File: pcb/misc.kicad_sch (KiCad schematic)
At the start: 11 parts, among them U3 ESP32-C3-MINI-1

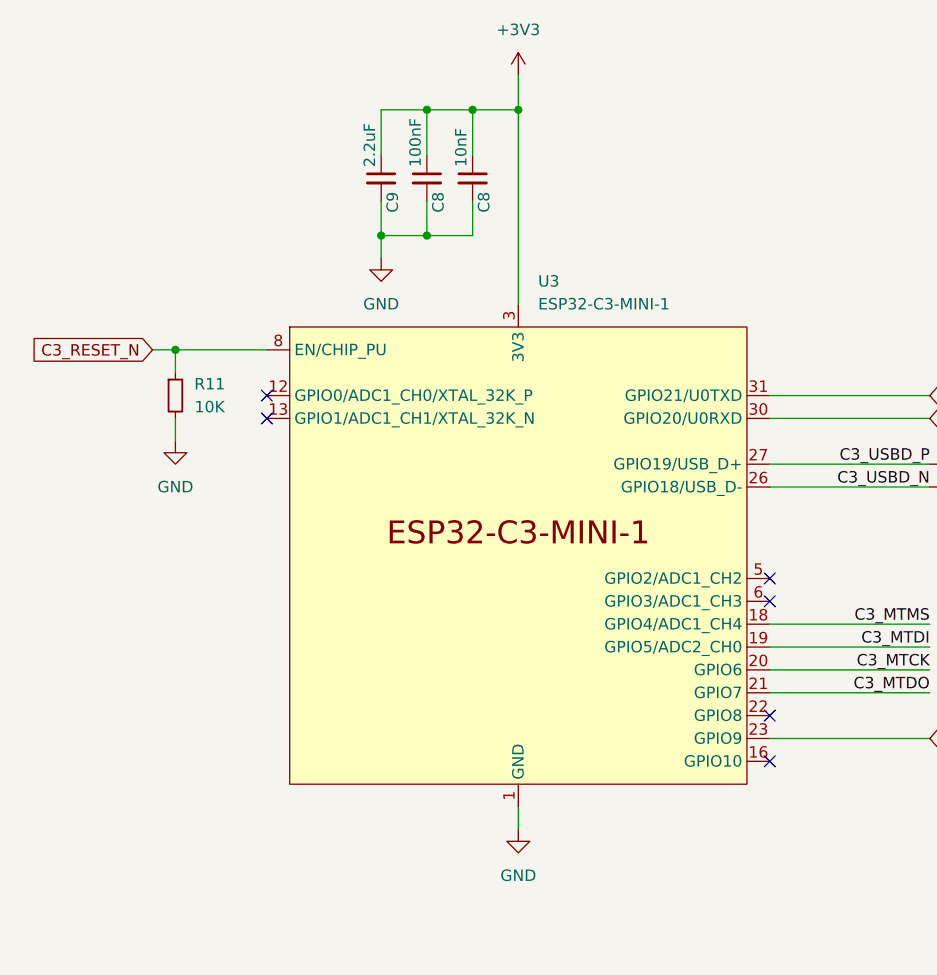
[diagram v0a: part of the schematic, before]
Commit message: pcb: Add part numbers for passives
Change-Id: Ie1730dd2a7126b7f6f602689064a4dbf8996e7b6
Reviewed-on: https://pigweed-review.googlesource.com/c/pigweed/kudzu/+/172895
Reviewed-by: Anthony DiGirolamo <anthony.digirolamo@gmail.com>
Reviewed-by: Anthony DiGirolamo <tonymd@google.com>
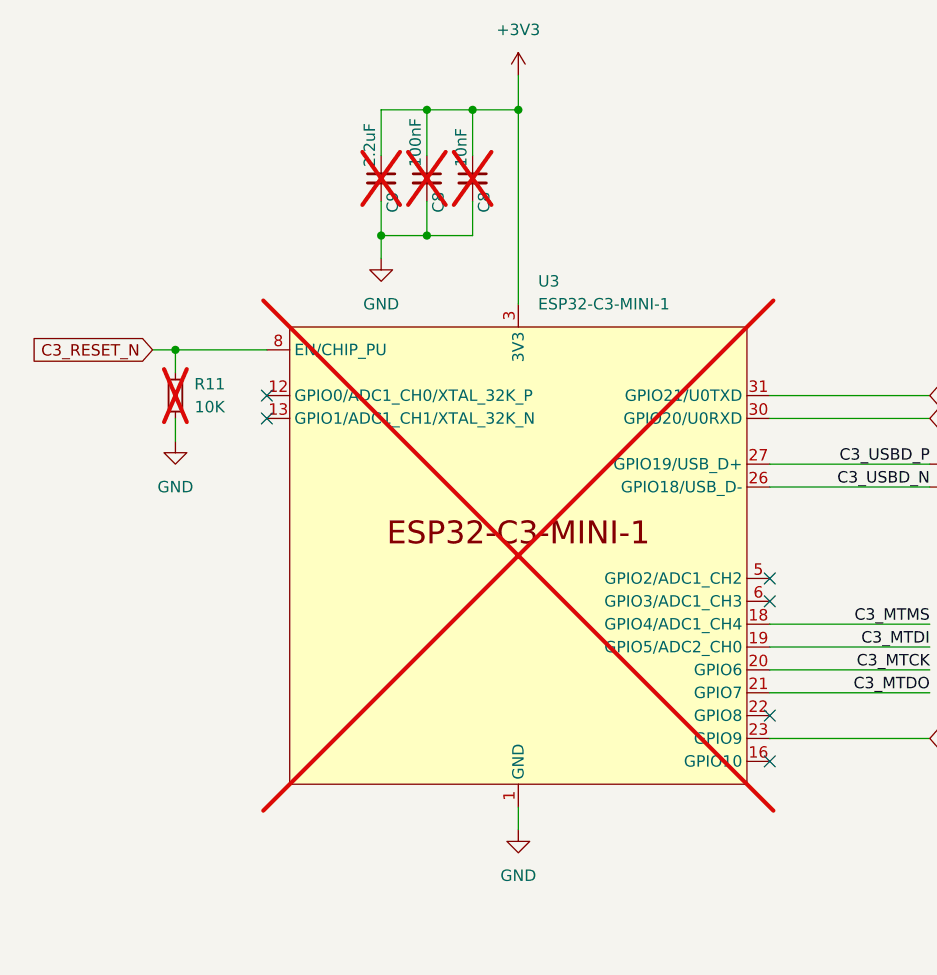
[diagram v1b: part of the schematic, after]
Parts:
- C8: DigiKey PN (none) -> 1276-1009-2-ND; Price @ 10 (none) -> 0.02500; Price @ 25 (none) -> 0.01340; now not fitted
- C8: DigiKey PN (none) -> 1276-1000-2-ND; Price @ 10 (none) -> 0.01200; Price @ 25 (none) -> 0.00856; now not fitted
- C9: DigiKey PN (none) -> 1276-1040-2-ND; Price @ 10 (none) -> 0.03460; Price @ 25 (none) -> 0.02830; now not fitted
- R11: DigiKey PN (none) -> RNCP0603FTD10K0TR-ND; Price @ 10 (none) -> 0.03240; Price @ 25 (none) -> 0.02380; now not fitted
- U3: now not fitted
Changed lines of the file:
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@@
   )
   (symbol (lib_id "Device:C_Small") (at 123.19 34.29 0) (unit 1)
-    (in_bom yes) (on_board yes) (dnp no)
+    (in_bom yes) (on_board yes) (dnp yes)
     (property "Reference" "C9" (at 124.46 38.1 90)
       (effects (font (size 1.27 1.27)) (justify left))
@@
       (effects (font (size 1.27 1.27)) hide)
     )
-    (property "Price @ 10" "" (at 123.19 34.29 0)
-      (effects (font (size 1.27 1.27)) hide)
-    )
-    (property "Price @ 25" "" (at 123.19 34.29 0)
+    (property "Price @ 10" "0.03460" (at 123.19 34.29 0)
+      (effects (font (size 1.27 1.27)) hide)
+    )
+    (property "Price @ 25" "0.02830" (at 123.19 34.29 0)
+      (effects (font (size 1.27 1.27)) hide)
+    )
+    (property "DigiKey PN" "1276-1040-2-ND" (at 123.19 34.29 0)
       (effects (font (size 1.27 1.27)) hide)
     )
@@
   )
   (symbol (lib_id "Device:C_Small") (at 133.35 34.29 0) (unit 1)
-    (in_bom yes) (on_board yes) (dnp no)
+    (in_bom yes) (on_board yes) (dnp yes)
     (property "Reference" "C8" (at 134.62 38.1 90)
       (effects (font (size 1.27 1.27)) (justify left))
@@
       (effects (font (size 1.27 1.27)) hide)
     )
-    (property "Price @ 10" "" (at 133.35 34.29 0)
-      (effects (font (size 1.27 1.27)) hide)
-    )
-    (property "Price @ 25" "" (at 133.35 34.29 0)
+    (property "Price @ 10" "0.02500" (at 133.35 34.29 0)
+      (effects (font (size 1.27 1.27)) hide)
+    )
+    (property "Price @ 25" "0.01340" (at 133.35 34.29 0)
+      (effects (font (size 1.27 1.27)) hide)
+    )
+    (property "DigiKey PN" "1276-1009-2-ND" (at 133.35 34.29 0)
       (effects (font (size 1.27 1.27)) hide)
     )
@@
   )
   (symbol (lib_id "Device:R_Small") (at 100.33 58.42 0) (unit 1)
-    (in_bom yes) (on_board yes) (dnp no)
+    (in_bom yes) (on_board yes) (dnp yes)
     (property "Reference" "R11" (at 104.14 57.15 0)
       (effects (font (size 1.27 1.27)))
@@
       (effects (font (size 1.27 1.27)) hide)
     )
-    (property "Price @ 10" "" (at 100.33 58.42 0)
-      (effects (font (size 1.27 1.27)) hide)
-    )
-    (property "Price @ 25" "" (at 100.33 58.42 0)
+    (property "Price @ 10" "0.03240" (at 100.33 58.42 0)
+      (effects (font (size 1.27 1.27)) hide)
+    )
+    (property "Price @ 25" "0.02380" (at 100.33 58.42 0)
+      (effects (font (size 1.27 1.27)) hide)
+    )
+    (property "DigiKey PN" "RNCP0603FTD10K0TR-ND" (at 100.33 58.42 0)
       (effects (font (size 1.27 1.27)) hide)
     )
@@
   )
   (symbol (lib_id "Espressif:ESP32-C3-MINI-1") (at 138.43 76.2 0) (unit 1)
-    (in_bom yes) (on_board yes) (dnp no) (fields_autoplaced)
+    (in_bom yes) (on_board yes) (dnp yes) (fields_autoplaced)
     (property "Reference" "U3" (at 140.6241 45.72 0)
       (effects (font (size 1.27 1.27)) (justify left))
@@
   )
   (symbol (lib_id "Device:C_Small") (at 128.27 34.29 0) (unit 1)
-    (in_bom yes) (on_board yes) (dnp no)
+    (in_bom yes) (on_board yes) (dnp yes)
     (property "Reference" "C8" (at 129.54 38.1 90)
       (effects (font (size 1.27 1.27)) (justify left))
@@
       (effects (font (size 1.27 1.27)) hide)
     )
-    (property "Price @ 10" "" (at 128.27 34.29 0)
-      (effects (font (size 1.27 1.27)) hide)
-    )
-    (property "Price @ 25" "" (at 128.27 34.29 0)
-      (effects (font (size 1.27 1.27)) hide)
-    )
+    (property "Price @ 10" "0.01200" (at 128.27 34.29 0)
+      (effects (font (size 1.27 1.27)) hide)
+    )
+    (property "Price @ 25" "0.00856" (at 128.27 34.29 0)
+      (effects (font (size 1.27 1.27)) hide)
+    )
+    (property "DigiKey PN" "1276-1000-2-ND" (at 128.27 34.29 0)
+      (effects (font (size 1.27 1.27)) hide)
+    )
